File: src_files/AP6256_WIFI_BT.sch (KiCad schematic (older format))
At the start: 20 parts

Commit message: wifi module complete
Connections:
- net BT_REG_ON_H_GPIO2_B7: no longer U?.12 (WL_REG_ON)
- new net WIFI_REG_ON_H_GPIO2_B1: U?.12 (WL_REG_ON)
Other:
- note added: "Z0 = 50 Ohms"
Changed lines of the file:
@@
 $Descr A4 11693 8268
 encoding utf-8
-Sheet 7 7
+Sheet 8 8
 Title ""
 Date ""
@@
 	3925 2650 3775 2650
 Text HLabel 3775 2750 0    33   Input ~ 0
-BT_REG_ON_H_GPIO2_B7
+WIFI_REG_ON_H_GPIO2_B1
 Wire Wire Line
 	3925 2750 3775 2750
@@
 Wire Wire Line
 	5875 4000 6275 4000
+Wire Notes Line
+	1050 1375 1050 1625
+Wire Notes Line
+	1050 1625 3250 1625
+Text Notes 2350 1625 0    39   ~ 0
+Z0 = 50 Ohms
 $EndSCHEMATC

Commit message: littleupdate
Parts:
- C75, C76, C77, C78, C79, C80, C81, C82, C83: renamed from C?; footprint (none) -> Capacitor_SMD:C_0402_1005Metric
- FB1: renamed from FB?; footprint (none) -> Inductor_SMD:L_0603_1608Metric
- FB2: renamed from FB?; footprint (none) -> Inductor_SMD:L_0201_0603Metric
- L9: renamed from L?; footprint (none) -> greencharge-footprints:S6125-M2-3.0A
- R15, R16, R17, R18, R19: renamed from R?; footprint (none) -> Resistor_SMD:R_0402_1005Metric
- U3: renamed from U?; footprint (none) -> Package_DFN_QFN:QFN-44-1EP_8x8mm_P0.65mm_EP6.45x6.45mm
- Y2: renamed from Y?; footprint (none) -> Crystal:Crystal_SMD_3225-4Pin_3.2x2.5mm_HandSoldering
- gave numbers to parts that had none: 1
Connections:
- net GND: now also C78.2

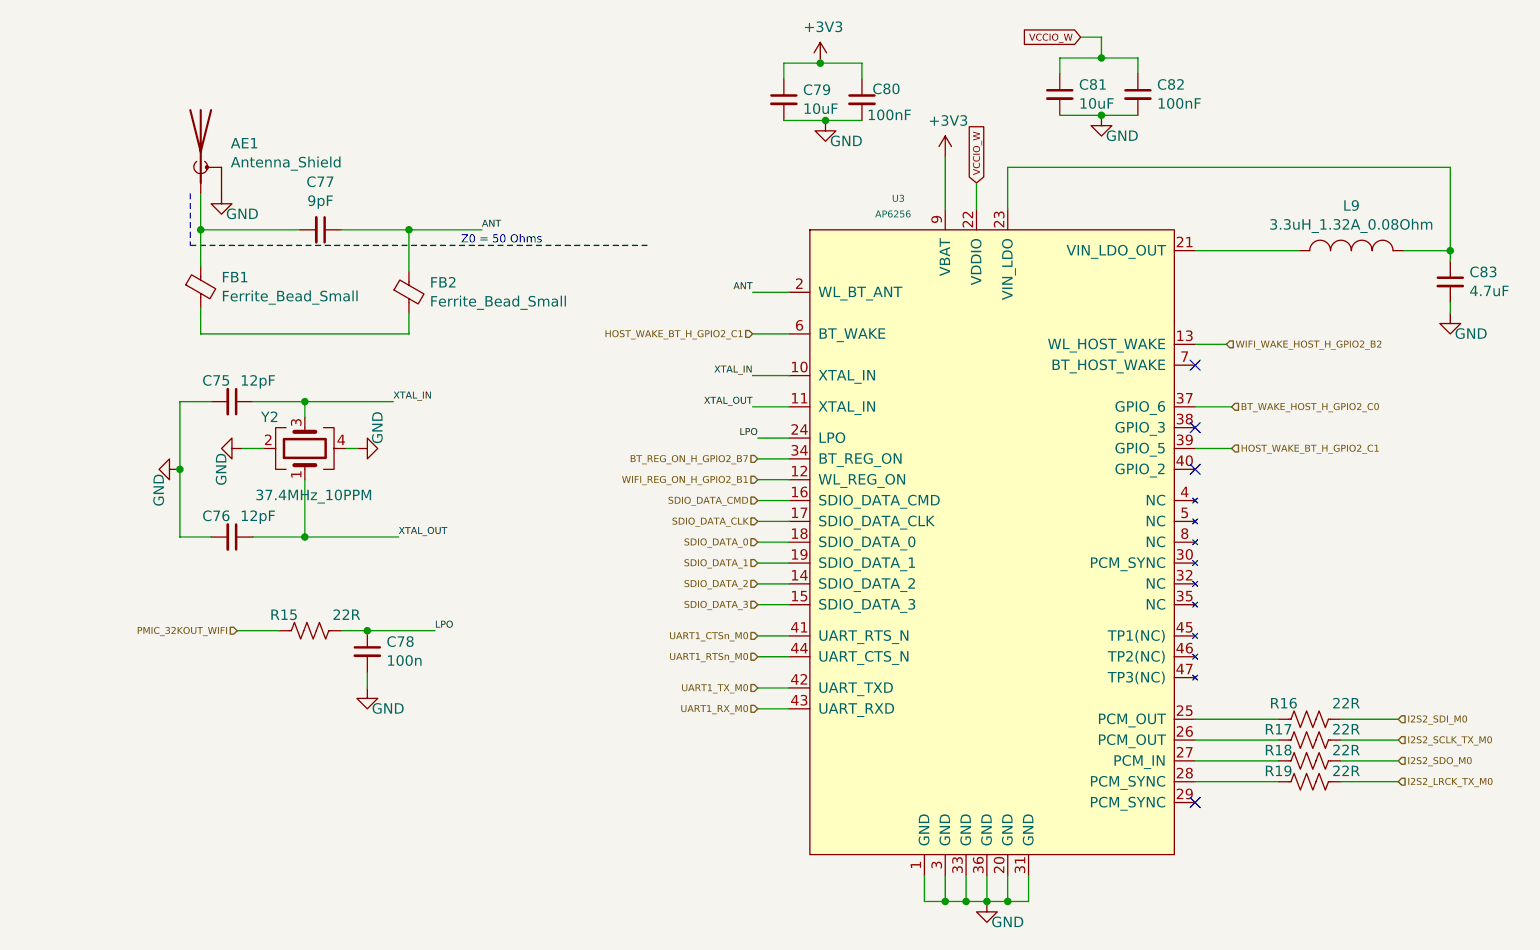
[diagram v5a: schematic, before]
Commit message: schematic capture complete
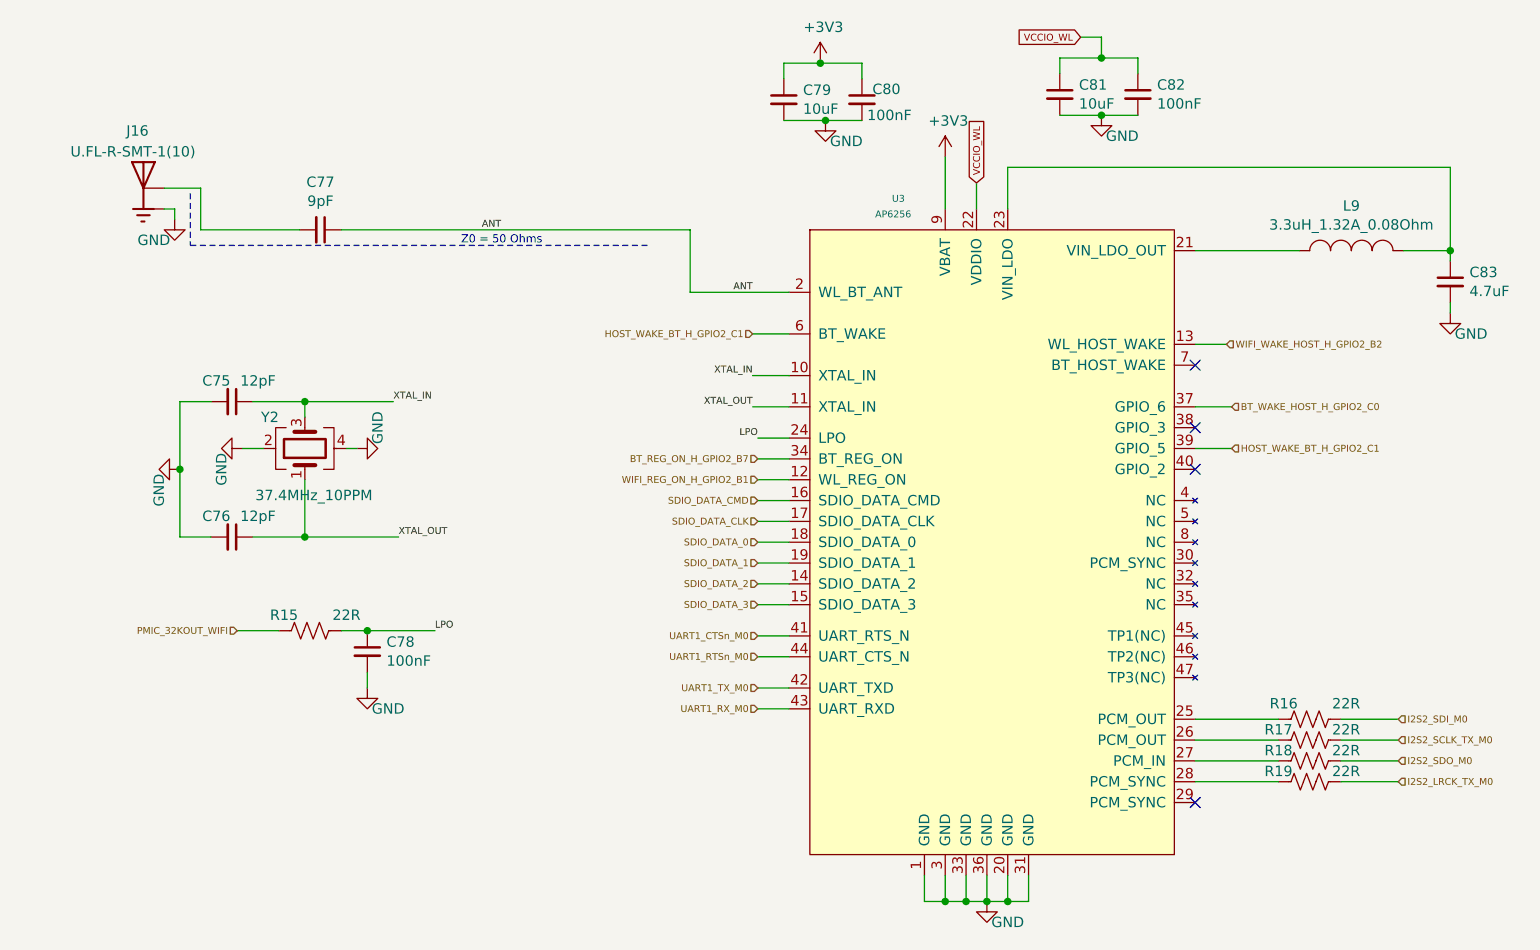
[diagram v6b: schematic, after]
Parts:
- removed AE1: Antenna_Shield, symbol Device:Antenna_Shield
- removed FB1: Ferrite_Bead_Small, Inductor_SMD:L_0603_1608Metric, symbol Device:Ferrite_Bead_Small
- removed FB2: Ferrite_Bead_Small, Inductor_SMD:L_0201_0603Metric, symbol Device:Ferrite_Bead_Small
- added J16: U.FL-R-SMT-1(10), greencharge-footprints:HRS_U.FL-R-SMT-1(10), symbol U.FL-R-SMT-1_10_:U.FL-R-SMT-1(10)
- C78: value 100n -> 100nF
- L9: footprint greencharge-footprints:S6125-M2-3.0A -> greencharge-footprints:SNR3015K-3R3M; MPN (none) -> SNR3015K-3R3M
- U3: footprint Package_DFN_QFN:QFN-44-1EP_8x8mm_P0.65mm_EP6.45x6.45mm -> greencharge-footprints:ap6256_QFN-44_12.5x12.5_Pitch0.9mm
- Y2: footprint Crystal:Crystal_SMD_3225-4Pin_3.2x2.5mm_HandSoldering -> Crystal:Crystal_SMD_2016-4Pin_2.0x1.6mm; MPN (none) -> XRCGB37M400F1S1AR0
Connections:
- net GND: now also J16.1, J16.3
- net at C77.2: now also J16.2
- net VCCIO_W renamed VCCIO_WL
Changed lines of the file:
@@
 $Descr A4 11693 8268
 encoding utf-8
-Sheet 6 13
+Sheet 5 15
 Title ""
 Date ""
@@
 $EndDescr
 $Comp
-L Device:Antenna_Shield AE?
-U 1 1 629B6A49
-P 1100 1175
-AR Path="/629B6A49" Ref="AE?"  Part="1"
-AR Path="/629B27D4/629B6A49" Ref="AE1"  Part="1"
-F 0 "AE1" H 1244 1214 50  0000 L CNN
-F 1 "Antenna_Shield" H 1244 1123 50  0000 L CNN
-F 2 "" H 1100 1275 50  0001 C CNN
-F 3 "~" H 1100 1275 50  0001 C CNN
-	1    1100 1175
-	1    0    0    -1
-$EndComp
-$Comp
 L Device:C_Small C?
 U 1 1 629B6A4F
@@
 $EndComp
 Wire Wire Line
-	1100 1375 1100 1550
-Wire Wire Line
 	1100 1550 1575 1550
-$Comp
-L Device:Ferrite_Bead_Small FB?
-U 1 1 629B6A57
-P 1100 1825
-AR Path="/629B6A57" Ref="FB?"  Part="1"
-AR Path="/629B27D4/629B6A57" Ref="FB1"  Part="1"
-F 0 "FB1" H 1200 1871 50  0000 L CNN
-F 1 "Ferrite_Bead_Small" H 1200 1780 50  0000 L CNN
-F 2 "Inductor_SMD:L_0603_1608Metric" V 1030 1825 50  0001 C CNN
-F 3 "~" H 1100 1825 50  0001 C CNN
-	1    1100 1825
-	1    0    0    -1
-$EndComp
-$Comp
-L Device:Ferrite_Bead_Small FB?
-U 1 1 629B6A5D
-P 2100 1850
-AR Path="/629B6A5D" Ref="FB?"  Part="1"
-AR Path="/629B27D4/629B6A5D" Ref="FB2"  Part="1"
-F 0 "FB2" H 2200 1896 50  0000 L CNN
-F 1 "Ferrite_Bead_Small" H 2200 1805 50  0000 L CNN
-F 2 "Inductor_SMD:L_0201_0603Metric" V 2030 1850 50  0001 C CNN
-F 3 "~" H 2100 1850 50  0001 C CNN
-	1    2100 1850
-	1    0    0    -1
-$EndComp
-Wire Wire Line
-	2100 1750 2100 1550
-Wire Wire Line
-	2100 1550 1775 1550
-Wire Wire Line
-	1100 1725 1100 1550
-Connection ~ 1100 1550
-Wire Wire Line
-	1100 1925 1100 2050
-Wire Wire Line
-	1100 2050 2100 2050
-Wire Wire Line
-	2100 2050 2100 1950
-Wire Wire Line
-	2100 1550 2450 1550
-Connection ~ 2100 1550
 Text Label 2450 1550 0    33   ~ 0
 ANT
@@
 F 0 "Y2" V 1750 2725 50  0000 L CNN
 F 1 "37.4MHz_10PPM" V 1375 2275 50  0000 L CNN
-F 2 "Crystal:Crystal_SMD_3225-4Pin_3.2x2.5mm_HandSoldering" H 1600 2600 50  0001 C CNN
+F 2 "Crystal:Crystal_SMD_2016-4Pin_2.0x1.6mm" H 1600 2600 50  0001 C CNN
 F 3 "~" H 1600 2600 50  0001 C CNN
+F 4 "XRCGB37M400F1S1AR0" V 1600 2600 50  0001 C CNN "MPN"
 	1    1600 2600
 	0    -1   -1   0
@@
 	3925 2050 3750 2050
 Wire Wire Line
-	3925 1850 3750 1850
-Wire Wire Line
 	4875 4650 4875 4775
 Wire Wire Line
@@
 F 0 "U3" H 4450 1400 33  0000 C CNN
 F 1 "AP6256" H 4425 1325 33  0000 C CNN
-F 2 "Package_DFN_QFN:QFN-44-1EP_8x8mm_P0.65mm_EP6.45x6.45mm" H 4275 1400 33  0001 C CNN
+F 2 "greencharge-footprints:ap6256_QFN-44_12.5x12.5_Pitch0.9mm" H 4275 1400 33  0001 C CNN
 F 3 "" H 4275 1400 33  0001 C CNN
 	1    4275 1400
@@
 P 1900 3575
 F 0 "C78" H 1992 3621 50  0000 L CNN
-F 1 "100n" H 1992 3530 50  0000 L CNN
+F 1 "100nF" H 1992 3530 50  0000 L CNN
 F 2 "Capacitor_SMD:C_0402_1005Metric" H 1900 3575 50  0001 C CNN
 F 3 "~" H 1900 3575 50  0001 C CNN
@@
 $Comp
 L OLIMEX_Power:GND #PWR?
-U 1 1 629B6A92
-P 1200 1375
-AR Path="/629B6A92" Ref="#PWR?"  Part="1"
-AR Path="/629B27D4/629B6A92" Ref="#PWR0180"  Part="1"
-F 0 "#PWR0180" H 1200 1125 50  0001 C CNN
-F 1 "GND" H 1300 1275 50  0000 C CNN
-F 2 "" H 1200 1375 60  0000 C CNN
-F 3 "" H 1200 1375 60  0000 C CNN
-	1    1200 1375
-	1    0    0    -1
-$EndComp
-$Comp
-L OLIMEX_Power:GND #PWR?
 U 1 1 629F302E
 P 4100 1025
@@
 F 0 "L9" H 6625 1865 50  0000 C CNN
 F 1 "3.3uH_1.32A_0.08Ohm" H 6625 1774 50  0000 C CNN
-F 2 "greencharge-footprints:S6125-M2-3.0A" H 6625 1650 60  0001 C CNN
+F 2 "greencharge-footprints:SNR3015K-3R3M" H 6625 1650 60  0001 C CNN
 F 3 "" H 6625 1650 60  0000 C CNN
+F 4 "SNR3015K-3R3M" H 6625 1650 50  0001 C CNN "MPN"
 	1    6625 1650
 	1    0    0    -1
@@
 	5425 1000 5600 1000
 Text GLabel 4825 1325 1    33   Input ~ 0
-VCCIO_W
+VCCIO_WL
 Text GLabel 5325 625  0    33   Input ~ 0
-VCCIO_W
+VCCIO_WL
 Wire Wire Line
 	5225 725  5425 725
@@
 Wire Wire Line
 	1900 3750 1900 3675
+$Comp
+L U.FL-R-SMT-1_10_:U.FL-R-SMT-1(10) J?
+U 1 1 61E5D3CF
+P 825 1350
+AR Path="/64C7F7B0/61E5D3CF" Ref="J?"  Part="1"
+AR Path="/629B27D4/61E5D3CF" Ref="J16"  Part="1"
+F 0 "J16" H 800 1625 50  0000 L CNN
+F 1 "U.FL-R-SMT-1(10)" H 575 1525 50  0000 L CNN
+F 2 "greencharge-footprints:HRS_U.FL-R-SMT-1(10)" H 825 1350 50  0001 L BNN
+F 3 "" H 825 1350 50  0001 L BNN
+F 4 "U.FL Series 6 Ghz 50 Ohm Ultra-small SMT Coaxial Cable Receptacle" H 825 1350 50  0001 L BNN "DESCRIPTION"
+F 5 "Manufacturer Recommendation" H 825 1350 50  0001 L BNN "STANDARD"
+F 6 "Good" H 825 1350 50  0001 L BNN "AVAILABILITY"
+F 7 "0.71 USD" H 825 1350 50  0001 L BNN "PRICE"
+F 8 "Hirose" H 825 1350 50  0001 L BNN "MANUFACTURER"
+F 9 "U.FL-R-SMT-1_10_" H 825 1350 50  0001 L BNN "MPN"
+F 10 "None" H 825 1350 50  0001 L BNN "PACKAGE"
+	1    825  1350
+	-1   0    0    -1
+$EndComp
+$Comp
+L OLIMEX_Power:GND #PWR?
+U 1 1 61E5D3D5
+P 975 1500
+AR Path="/61E5D3D5" Ref="#PWR?"  Part="1"
+AR Path="/64C7F7B0/61E5D3D5" Ref="#PWR?"  Part="1"
+AR Path="/629B27D4/61E5D3D5" Ref="#PWR0279"  Part="1"
+F 0 "#PWR0279" H 975 1250 50  0001 C CNN
+F 1 "GND" H 875 1400 50  0000 C CNN
+F 2 "" H 975 1500 60  0000 C CNN
+F 3 "" H 975 1500 60  0000 C CNN
+	1    975  1500
+	1    0    0    -1
+$EndComp
+Wire Wire Line
+	925  1450 975  1450
+Wire Wire Line
+	975  1450 975  1500
+Wire Wire Line
+	1100 1350 925  1350
+Wire Wire Line
+	1100 1350 1100 1550
+Wire Wire Line
+	3450 1550 3450 1850
+Wire Wire Line
+	3450 1850 3925 1850
+Wire Wire Line
+	1775 1550 3450 1550
 $EndSCHEMATC
